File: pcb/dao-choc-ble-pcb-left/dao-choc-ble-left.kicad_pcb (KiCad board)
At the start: 2 copper layers, 150 x 85.7 mm, 85 parts, among them J1 USB, J2 PROG, K1 KEY_SWITCH, K10 KEY_SWITCH, K11 KEY_SWITCH, K12 KEY_SWITCH, K13 KEY_SWITCH, K14 KEY_SWITCH, K15 KEY_SWITCH, K16 KEY_SWITCH, K17 KEY_SWITCH, K18 KEY_SWITCH, K19 KEY_SWITCH, K2 KEY_SWITCH, K20 KEY_SWITCH, K21 KEY_SWITCH, K22 KEY_SWITCH, K3 KEY_SWITCH, K4 KEY_SWITCH, K5 KEY_SWITCH, K6 KEY_SWITCH, K7 KEY_SWITCH, K8 KEY_SWITCH, K9 KEY_SWITCH, Q1 AO3401A, SW1 ON_OFF, SW2 RESET, U1 MS88SF2, U2 USBLC6-2SC6, U3 XC6220, U4 MCP73831

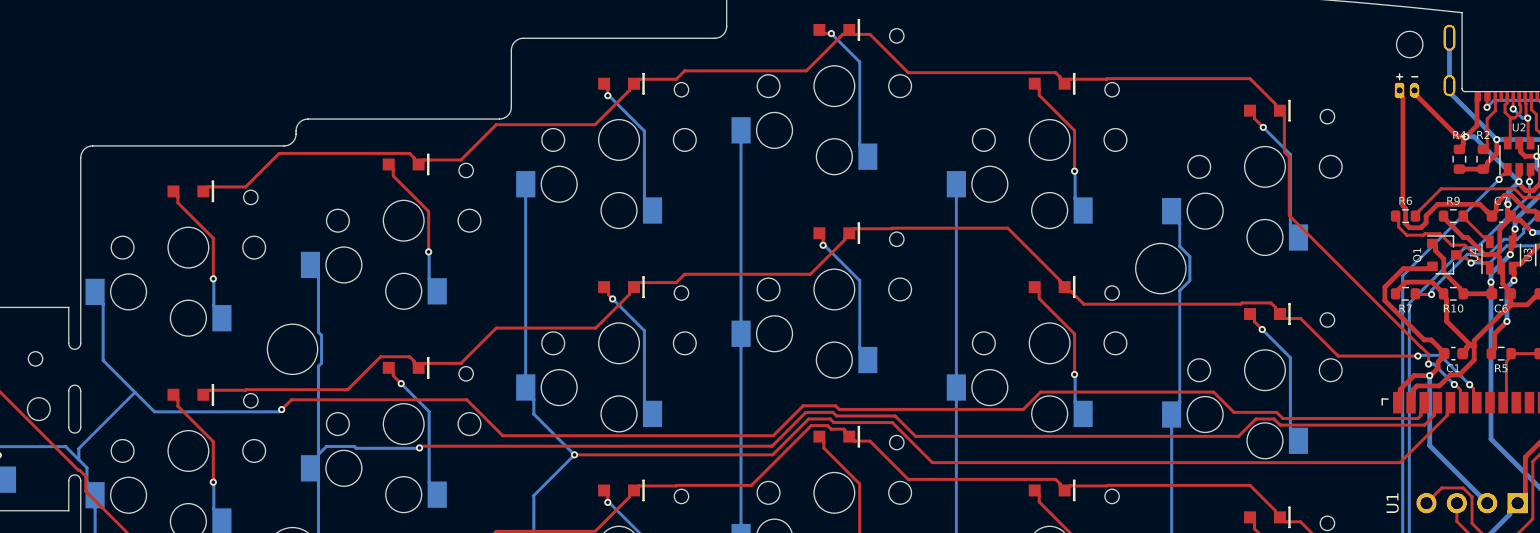
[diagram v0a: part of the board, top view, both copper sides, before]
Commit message: feature: changed footprint for battery connector
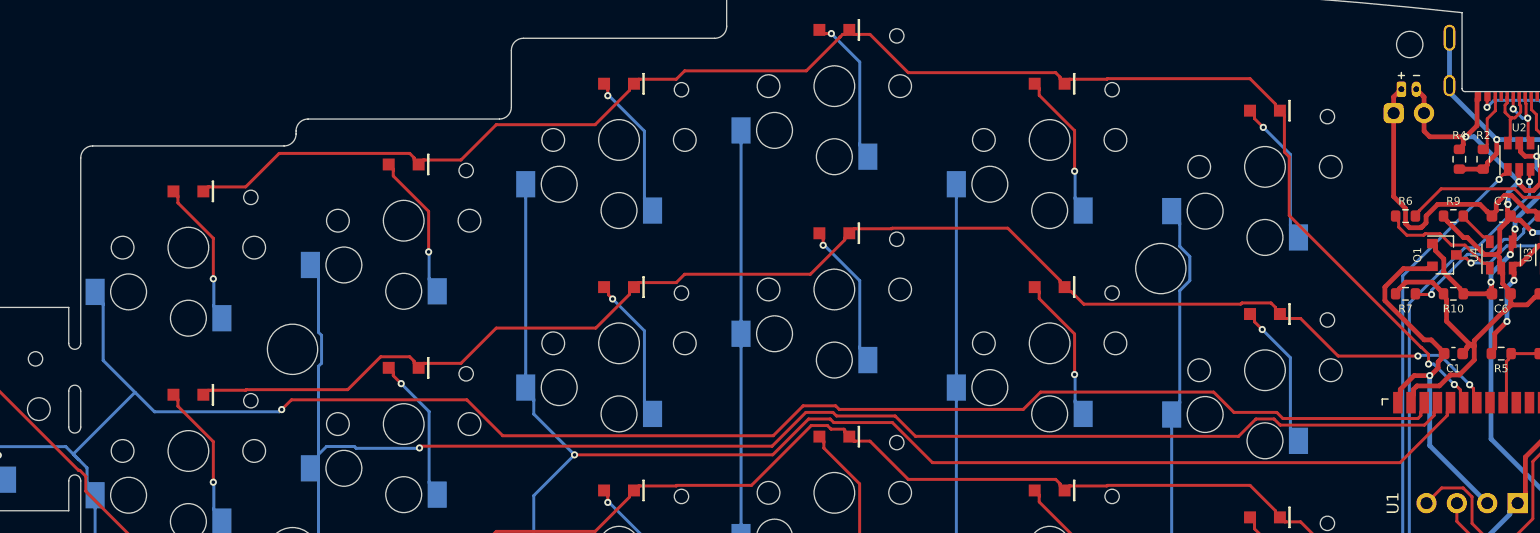
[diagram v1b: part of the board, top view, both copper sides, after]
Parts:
- moved BT1 0.18 mm to (110.4, -4.74)
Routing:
- net GND: track 122.9 -> 124.3 mm
- net VBAT: track 43.2 -> 43.9 mm
